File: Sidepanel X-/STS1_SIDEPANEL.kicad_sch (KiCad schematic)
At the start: 4 parts, among them J1 Conn_02x04_Odd_Even, J2 Conn_02x02_Odd_Even

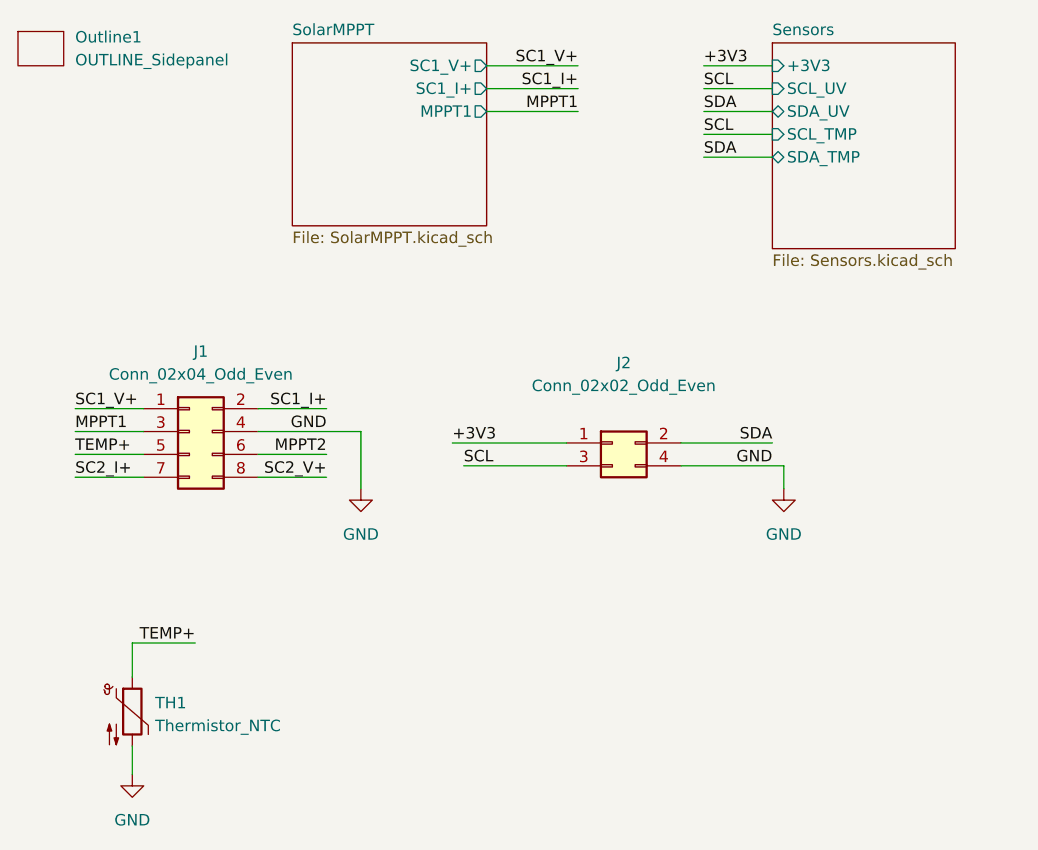
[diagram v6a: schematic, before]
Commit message: Adjusted the panel naming so that it conforms to the coordinate system convention governed by the Cubesat Design Specification.
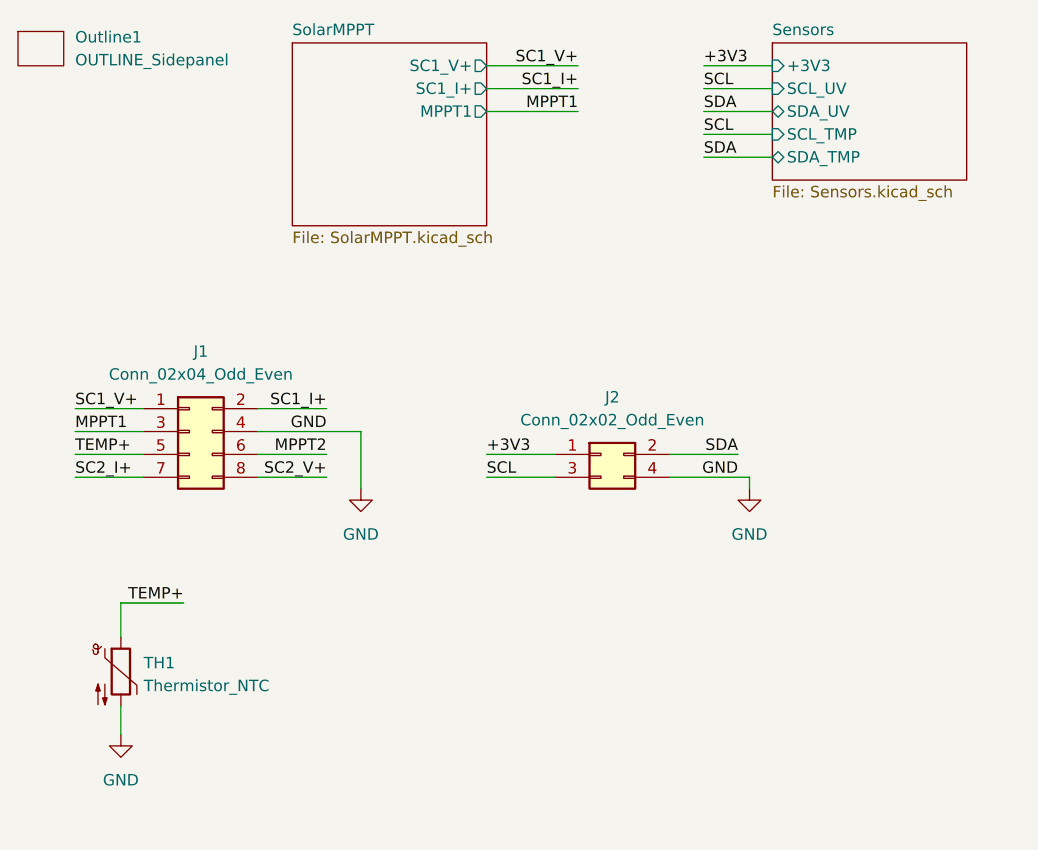
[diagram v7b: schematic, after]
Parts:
- Outline1: footprint USER_OUTLINE:OUTLINE_SidepanelX- -> USER_OUTLINE:OUTLINE_SidepanelX+
